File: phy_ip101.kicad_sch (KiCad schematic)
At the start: 48 parts, among them J1 8P8C, U4 IP101GRI, X1 ASE-xxxMHz

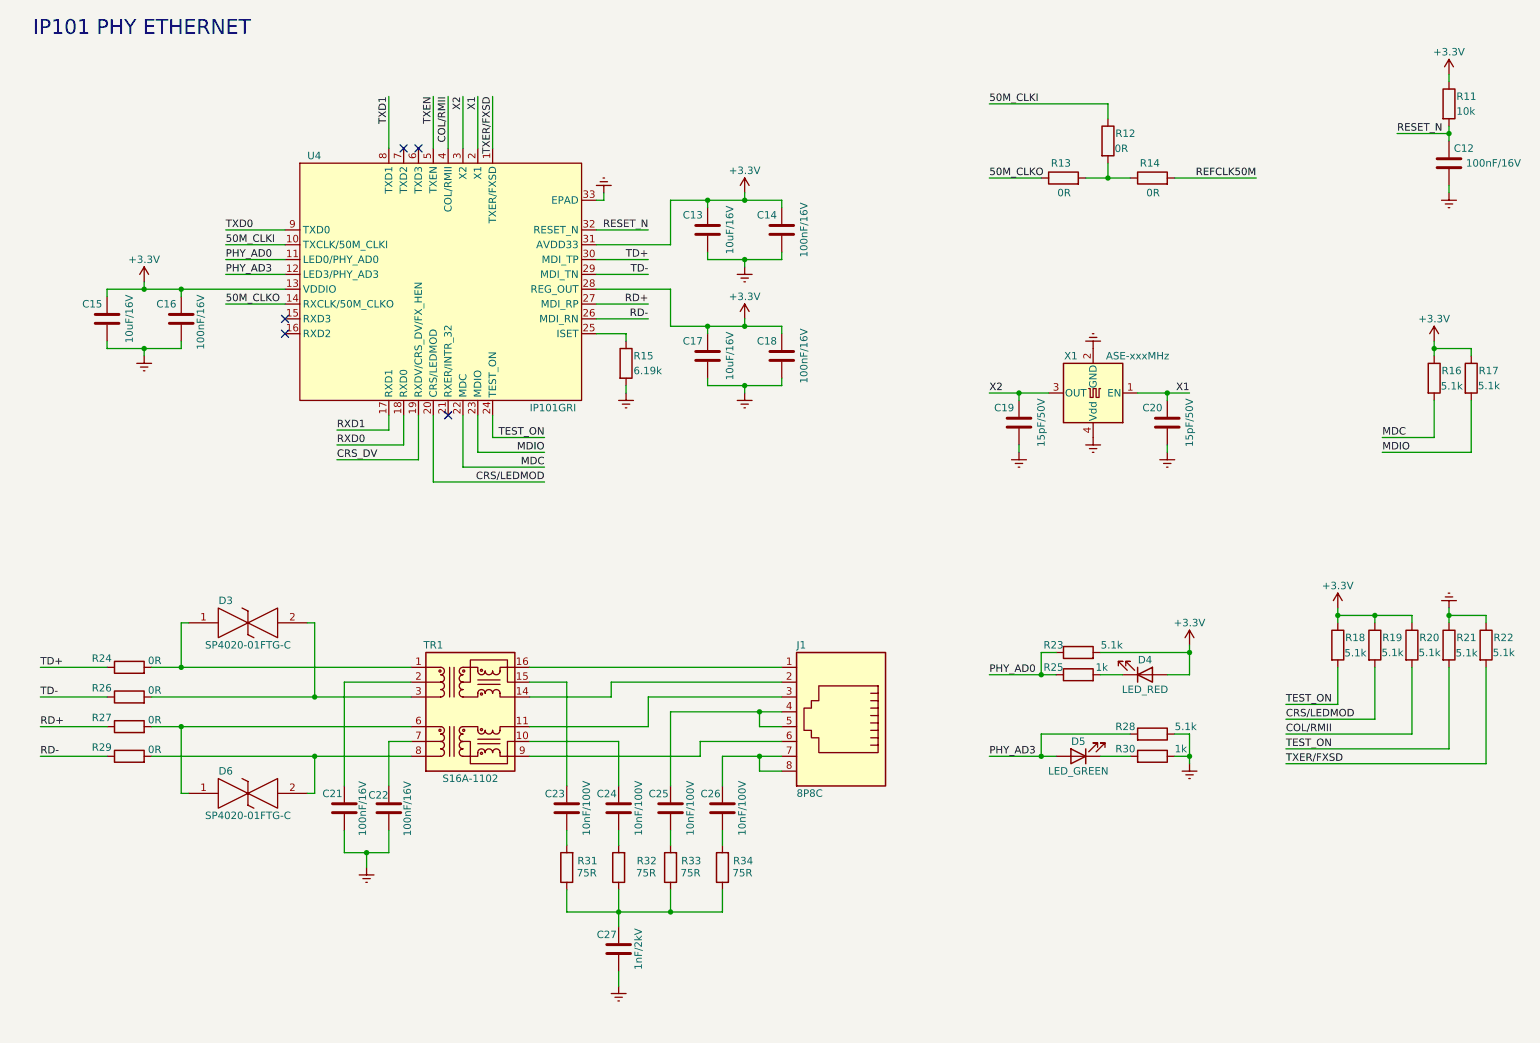
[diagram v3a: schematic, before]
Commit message: Adicionado hierarchical label
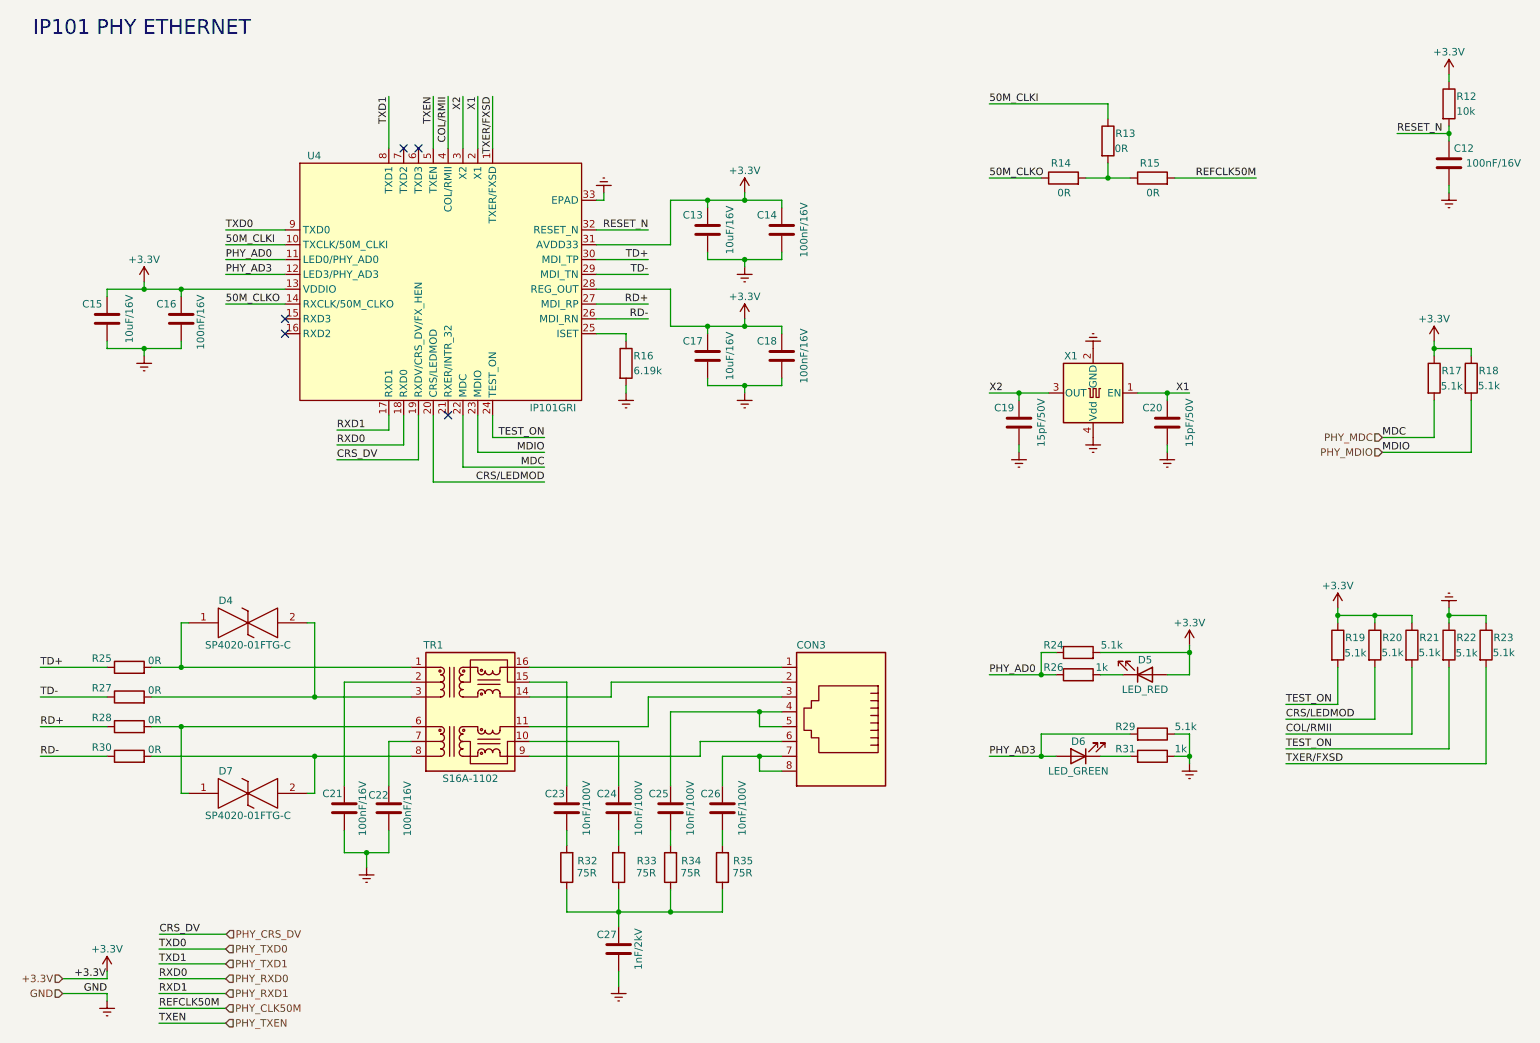
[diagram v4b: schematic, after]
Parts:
- CON3: renamed from J1; value 8P8C -> (none); footprint Connector_RJ:RJ45_OST_PJ012-8P8CX_Vertical -> (none)
- X1: value ASE-xxxMHz -> (none); footprint Oscillator:Oscillator_SMD_Abracon_ASE-4Pin_3.2x2.5mm -> (none)
- renumbered D3 to D4, D4 to D5, D5 to D6, D6 to D7, R11 to R12, R12 to R13, R13 to R14, R14 to R15, R15 to R16, R16 to R17, R17 to R18, R18 to R19, R19 to R20, R20 to R21, R21 to R22, R22 to R23, R23 to R24, R24 to R25, R25 to R26, R26 to R27, R27 to R28, R28 to R29, R29 to R30, R30 to R31, R31 to R32, R32 to R33, R33 to R34, R34 to R35
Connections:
- net CRS_DV renamed PHY_CRS_DV
- net MDC renamed PHY_MDC
- net MDIO renamed PHY_MDIO
- net REFCLK50M renamed PHY_CLK50M
- net RXD0 renamed PHY_RXD0
- net RXD1 renamed PHY_RXD1
- net TXD0 renamed PHY_TXD0
- net TXD1 renamed PHY_TXD1
- net TXEN renamed PHY_TXEN

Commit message: Cont. hierarchical label e descrição das folhas
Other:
- company: (none) -> Magalhaes
- title: Módulo Espressif -> PHY ETHERNET IP101
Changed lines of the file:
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@@
   (paper "A4")
   (title_block
-    (title "Módulo Espressif")
+    (title "PHY ETHERNET IP101")
     (date "2022-06-24")
-    (rev "v1.0")
+    (rev "0.0.0")
+    (company "Magalhaes")
+    (comment 1 "Author: Alexandre Magalhães")
+    (comment 2 "Variant 1: Full")
   )
   (junction (at 67.31 147.32) (diameter 0) (color 0 0 0 0)
